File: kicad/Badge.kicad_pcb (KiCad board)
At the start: 2 copper layers, 25 parts, among them SW1 SW_SPST, U1 LMC555xM

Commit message: routing 1
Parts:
- moved R8 189.2 mm to (52.1, 62.2), turned to 180 degrees
- moved JP2 187.2 mm to (77.5, 33.0)
- moved D7 181.9 mm to (55.9, 62.2), turned to 0 degrees
- moved R1 174.0 mm to (67.3, 39.4)
- moved R6 172.7 mm to (68.6, 57.1), turned to 180 degrees
- moved R3 172.3 mm to (62.2, 74.9), turned to 180 degrees
- moved D1 171.2 mm to (67.3, 36.8), turned to 0 degrees
- moved D5 168.3 mm to (68.6, 59.7)
- moved D3 168.1 mm to (62.2, 77.5)
- moved R7 162.5 mm to (85.1, 47.0), turned to 90 degrees
- moved D6 156.8 mm to (87.6, 47.0), turned to 90 degrees
- moved JP1 155.9 mm to (111.8, 33.0)
- moved R2 147.4 mm to (96.5, 40.6)
- moved D2 144.9 mm to (96.5, 38.1), turned to 0 degrees
- moved R4 134.9 mm to (104.1, 63.5), turned to 180 degrees
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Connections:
- net Net-(BT1-+) renamed /BAT
- net Net-(D5-A) renamed /PULSE2H
- net Net-(JP2-C) renamed /PULSE2L
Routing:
- net VCC: track 0.00 -> 191.7 mm, vias 0 -> 8
- net /PULSE: track 0.00 -> 152.4 mm, vias 0 -> 5
- net /PULSE2H: track 0.00 -> 123.2 mm, vias 0 -> 4
- net /PULSE2L: track 0.00 -> 90.5 mm
- net /BAT: track 0.00 -> 56.4 mm
- net /TR: track 0.00 -> 13.4 mm
- net GND: track 0.00 -> 11.6 mm, vias 0 -> 2
- net Net-(D1-K): track 0.00 -> 2.59 mm
- net Net-(D4-K): track 0.00 -> 2.59 mm
- net Net-(D8-K): track 0.00 -> 2.55 mm
- net Net-(D5-K): track 0.00 -> 2.55 mm
- net Net-(D3-K): track 0.00 -> 2.55 mm
- net Net-(D6-K): track 0.00 -> 2.55 mm
- net Net-(D2-K): track 0.00 -> 2.55 mm
- net Net-(D7-K): track 0.00 -> 1.78 mm
- added copper zone on B.Cu, net GND
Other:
- board outline added: 109.3 x 57.3 mm
- board text added: "NJIT ECET 2024"

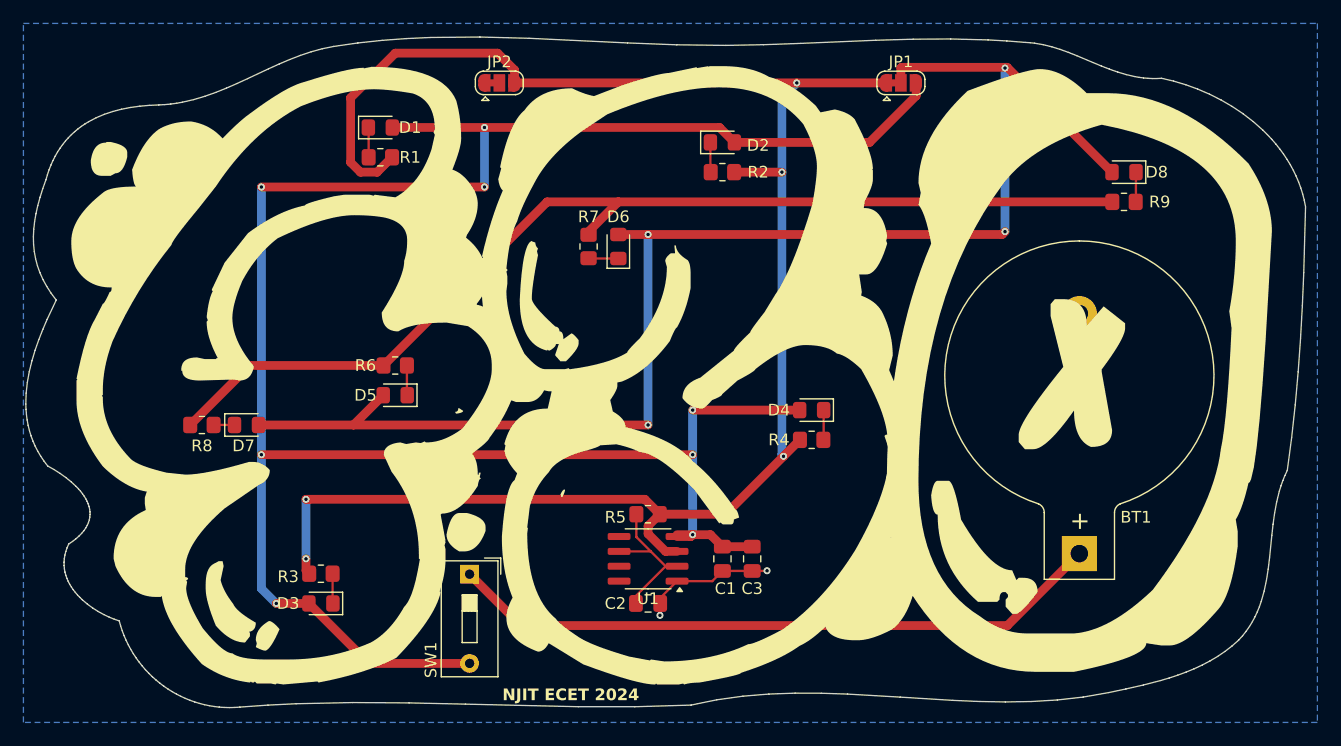
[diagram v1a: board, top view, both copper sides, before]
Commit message: fix routing, straight edge sections for solderpaste, milling gerbers
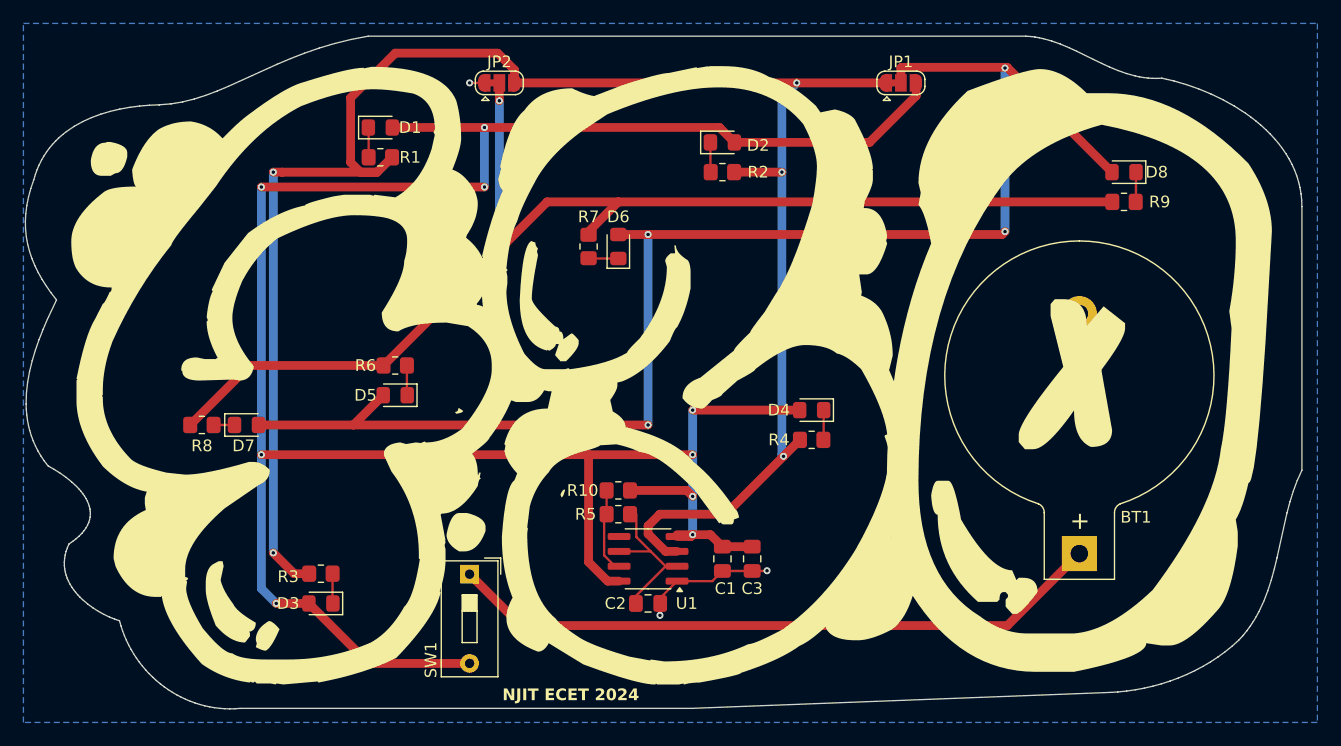
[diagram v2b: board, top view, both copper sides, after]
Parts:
- added R10: R, Resistor_SMD:R_0805_2012Metric_Pad1.20x1.40mm_HandSolder, F.Cu at (87.6, 67.8)
- moved R5 2.54 mm to (87.6, 69.8), turned to 0 degrees
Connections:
- R5 pad 1: /PULSE -> Net-(U1-DIS)
- U1 pad 7: unconnected-(U1-DIS-Pad7) -> Net-(U1-DIS)
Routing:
- net VCC: track 191.7 -> 209.7 mm, vias 8 -> 9
- net /PULSE2L: track 90.5 -> 104.7 mm, vias 0 -> 2
- net /PULSE: track 152.4 -> 160.4 mm
- net Net-(U1-DIS): track 0.00 -> 7.29 mm
- net GND: track 11.6 -> 12.8 mm, vias 2 -> 3
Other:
- board size 109.3 x 57.3 mm -> 109 x 57.4 mm

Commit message: fix discrepancies with milled board, to be milled again
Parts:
- R10: value R -> 22k
- R5: value R -> 100k
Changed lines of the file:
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@@
 		(tags "resistor handsolder")
 		(property "Reference" "R10"
-			(at 3.048 0 360)
+			(at 3.048 0 0)
 			(layer "F.SilkS")
 			(effects
@@
 			)
 		)
-		(property "Value" "R"
-			(at 0 1.65 360)
+		(property "Value" "22k"
+			(at 0 1.65 0)
 			(layer "F.Fab")
 			(effects
@@
 		)
 		(fp_text user "${REFERENCE}"
-			(at 0 0 360)
+			(at 0 0 0)
 			(layer "F.Fab")
 			(effects
@@
 		(tags "resistor handsolder")
 		(property "Reference" "R5"
-			(at -2.794 0 360)
+			(at -2.794 0 0)
 			(layer "F.SilkS")
 			(effects
@@
 			)
 		)
-		(property "Value" "R"
-			(at 0 1.65 360)
+		(property "Value" "100k"
+			(at 0 1.65 0)
 			(layer "F.Fab")
 			(effects
@@
 		)
 		(fp_text user "${REFERENCE}"
-			(at 0 0 360)
+			(at 0 0 0)
 			(layer "F.Fab")
 			(effects
